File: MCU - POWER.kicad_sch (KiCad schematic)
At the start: 22 parts, among them U1 STM32G474RET6, U2 STM32G474RET6

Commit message: [01/07/2026][MCU - IOs] Update
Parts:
- U1, U2: footprint (none) -> Duc_Library:LQFP-64_L10.0-W10.0-P0.50-LS12.0-BL; private Datasheet -> (none)
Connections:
- new net: C7., C9., FB1., U1.28 (VREF+), U1.29 (VDDA)
- new net: C14., C18., FB2., U2.28 (VREF+), U2.29 (VDDA)
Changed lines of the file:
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@@
 	(title_block
 		(title "MCU - POWER")
-		(date "2025-01-12")
+		(date "2026-06-27")
 		(rev "${REVISION}")
 		(company "${COMPANY}")
@@
 	)
 	(symbol
+		(lib_name "PBBHAQ2012H-102T10_1")
 		(lib_id "Duc_Library:PBBHAQ2012H-102T10")
 		(at 147.32 78.74 0)
@@
 	)
 	(symbol
-		(lib_name "PBBHAQ2012H-102T10_1")
 		(lib_id "Duc_Library:PBBHAQ2012H-102T10")
 		(at 147.32 144.78 0)
@@
 			)
 		)
-		(property private "Footprint" "Duc_Library:LQFP-64_L10.0-W10.0-P0.50-LS12.0-BL"
+		(property "Footprint" "Duc_Library:LQFP-64_L10.0-W10.0-P0.50-LS12.0-BL"
 			(at 225.552 98.044 0)
 			(effects
@@
 			)
 		)
-		(property private "Datasheet" "https://lcsc.com/product-detail/No-specification-for-star-making-plan_STMicroelectronics-STM32G474RET6_C521608.html"
+		(property "Datasheet" "https://lcsc.com/product-detail/No-specification-for-star-making-plan_STMicroelectronics-STM32G474RET6_C521608.html"
 			(at 233.68 100.33 0)
 			(do_not_autoplace yes)
@@
 			)
 		)
-		(property private "Footprint" "Duc_Library:LQFP-64_L10.0-W10.0-P0.50-LS12.0-BL"
+		(property "Footprint" "Duc_Library:LQFP-64_L10.0-W10.0-P0.50-LS12.0-BL"
 			(at 225.552 164.084 0)
 			(effects
@@
 			)
 		)
-		(property private "Datasheet" "https://lcsc.com/product-detail/No-specification-for-star-making-plan_STMicroelectronics-STM32G474RET6_C521608.html"
+		(property "Datasheet" "https://lcsc.com/product-detail/No-specification-for-star-making-plan_STMicroelectronics-STM32G474RET6_C521608.html"
 			(at 233.68 166.37 0)
 			(do_not_autoplace yes)
@@
 	)
 	(symbol
-		(lib_name "CC0402KRX7R6BB105_3")
+		(lib_name "CC0402KRX7R6BB105_5")
 		(lib_id "Duc_Library:CC0402KRX7R6BB105")
 		(at 182.88 114.3 90)
@@
 	)
 	(symbol
-		(lib_name "CC0402KRX7R9BB104_3")
+		(lib_name "CC0402KRX7R9BB104_2")
 		(lib_id "Duc_Library:CC0402KRX7R9BB104")
 		(at 182.88 152.4 90)
@@
 	)
 	(symbol
-		(lib_name "CC0402KRX7R9BB104_9")
+		(lib_name "CC0402KRX7R9BB104_8")
 		(lib_id "Duc_Library:CC0402KRX7R9BB104")
 		(at 182.88 86.36 90)
@@
 	)
 	(symbol
-		(lib_name "CC0402KRX7R9BB104_2")
+		(lib_name "CC0402KRX7R9BB104_4")
 		(lib_id "Duc_Library:CC0402KRX7R9BB104")
 		(at 182.88 134.62 90)
@@
 	)
 	(symbol
-		(lib_name "CC0402KRX7R9BB104_8")
+		(lib_name "CC0402KRX7R9BB104_7")
 		(lib_id "Duc_Library:CC0402KRX7R9BB104")
 		(at 162.56 134.62 90)
@@
 	)
 	(symbol
-		(lib_name "CC0402KRX7R9BB104_4")
+		(lib_name "CC0402KRX7R9BB104_9")
 		(lib_id "Duc_Library:CC0402KRX7R9BB104")
 		(at 162.56 68.58 90)
@@
 	)
 	(symbol
-		(lib_name "CC0402KRX7R9BB104_5")
+		(lib_name "CC0402KRX7R9BB104_3")
 		(lib_id "Duc_Library:CC0402KRX7R9BB104")
 		(at 139.7 68.58 90)
@@
 	)
 	(symbol
-		(lib_name "CC0402KRX7R6BB105_5")
+		(lib_name "CC0402KRX7R6BB105_3")
 		(lib_id "Duc_Library:CC0402KRX7R6BB105")
 		(at 160.02 152.4 90)
@@
 	)
 	(symbol
-		(lib_name "CC0402KRX7R9BB104_6")
+		(lib_name "CC0402KRX7R9BB104_5")
 		(lib_id "Duc_Library:CC0402KRX7R9BB104")
 		(at 182.88 68.58 90)
@@
 	)
 	(symbol
-		(lib_name "CC0402KRX7R9BB104_7")
+		(lib_name "CC0402KRX7R9BB104_6")
 		(lib_id "Duc_Library:CC0402KRX7R9BB104")
 		(at 116.84 134.62 90)

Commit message: Update Power Generation Schematic
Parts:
- removed U1, U2: STM32G474RET6, Duc_Library:LQFP-64_L10.0-W10.0-P0.50-LS12.0-BL, symbol Duc_Library:STM32G474RET6
- added U1, U2: STM32G474RET6, Duc_Library:LQFP-64_L10.0-W10.0-P0.50-LS12.0-BL, symbol Duc-MCUs:STM32G474RET6
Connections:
- net +3V3: now also U1.1 (VBAT), U1.16 (VDD), U1.32 (VDD), U1.48 (VDD), U1.64 (VDD), U2.1 (VBAT), U2.16 (VDD), U2.32 (VDD), U2.48 (VDD), U2.64 (VDD)
- net GND: now also U1.15 (VSS), U1.27 (VSSA), U1.31 (VSS), U1.47 (VSS), U1.63 (VSS), U2.15 (VSS), U2.27 (VSSA), U2.31 (VSS), U2.47 (VSS), U2.63 (VSS)
- new net: C7., C9., FB1., U1.28 (VREF+), U1.29 (VDDA)
- new net: C14., C18., FB2., U2.28 (VREF+), U2.29 (VDDA)
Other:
- title: MCU - POWER -> MCU - Power
- moved on the sheet: C1, C2, C3, C4, C5, C6, C7, C8, C9, FB1

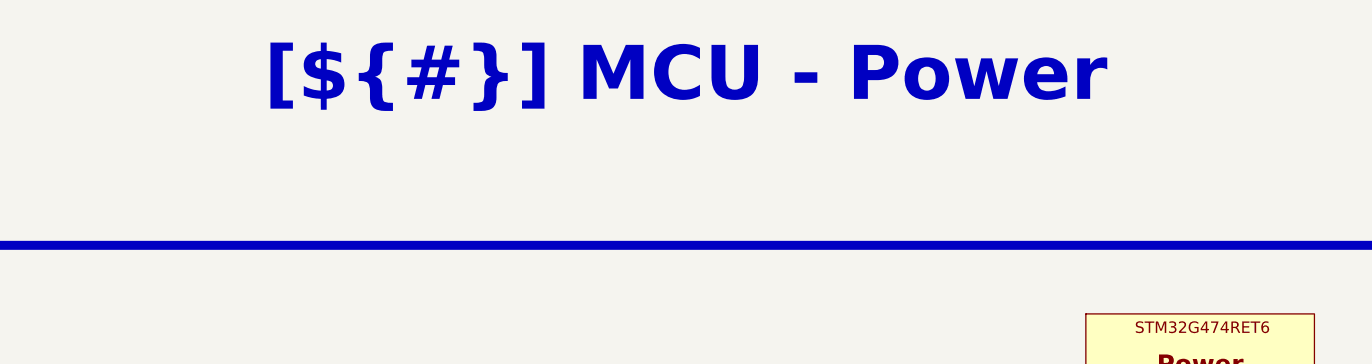
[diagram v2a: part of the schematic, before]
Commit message: Update Power Connector & Motor Control Schematic
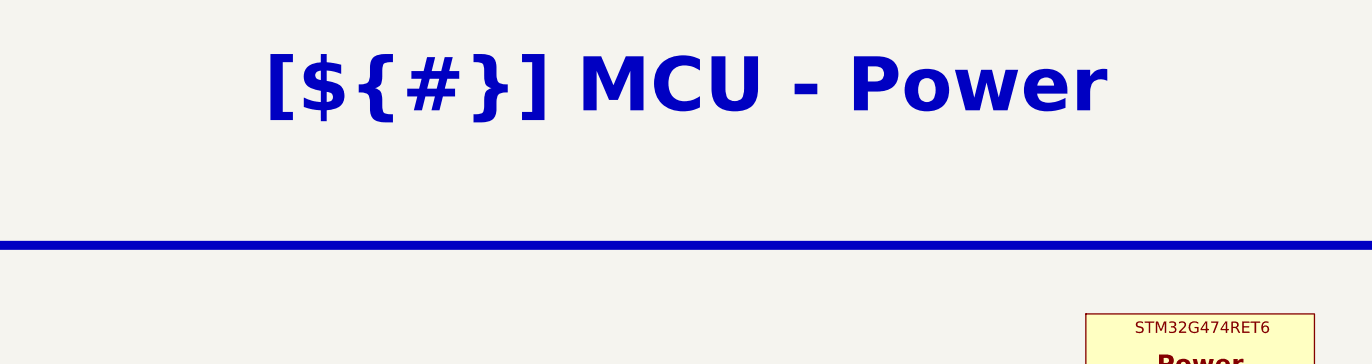
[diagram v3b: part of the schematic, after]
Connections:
- new net: C7., C9., FB1., U1.28 (VREF+), U1.29 (VDDA)
- new net: C14., C18., FB2., U2.28 (VREF+), U2.29 (VDDA)
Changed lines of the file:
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@@
 	(text_box "[${#}] ${TITLE}"
 		(exclude_from_sim no)
-		(at 12.7 12.7 0)
+		(at 12.7 13.97 0)
 		(size 393.7 12.7)
 		(margins 4.4999 4.4999 4.4999 4.4999)
